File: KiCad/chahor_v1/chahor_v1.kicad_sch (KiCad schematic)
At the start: 12 parts, among them SW1 RotaryEncoder, SW2 lower_case, SW3 upper_case, SW4 space, SW5 bcksp, SW6 ctrl, SW7 switch, SW8 navi_up, SW9 navi_down, U1 Keyboard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

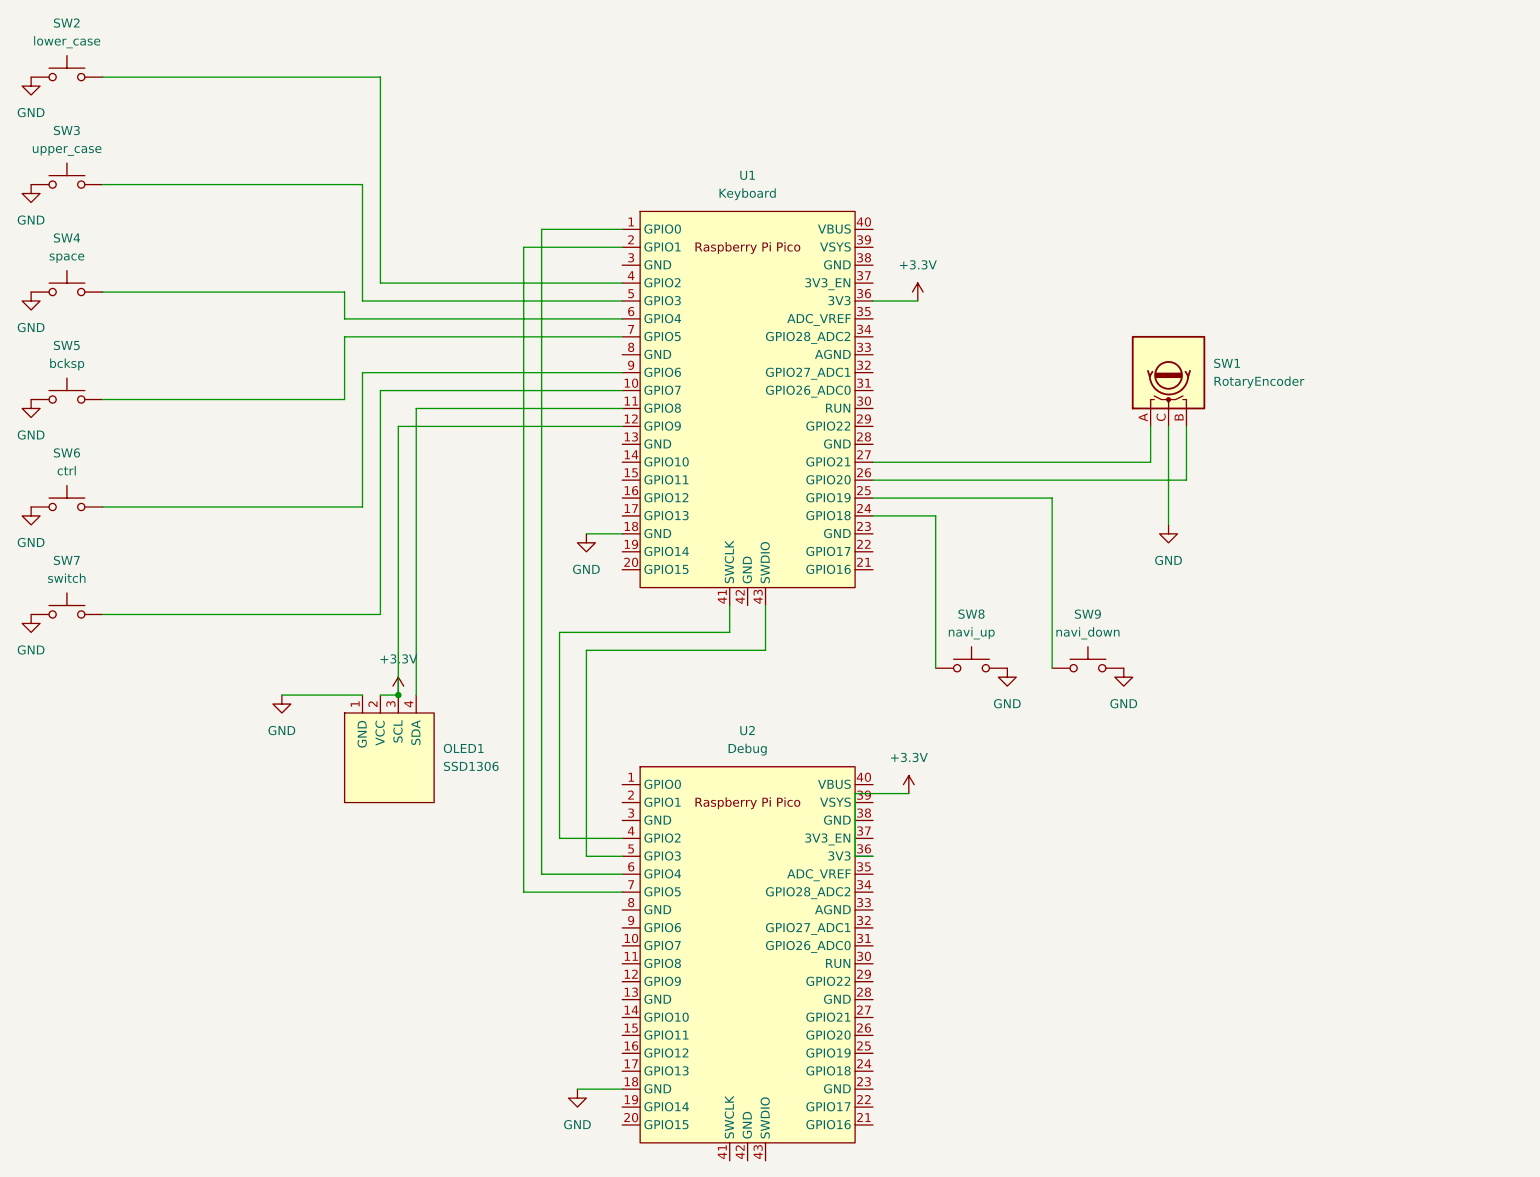
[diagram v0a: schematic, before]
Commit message: changed the production board to RP2040-Tiny
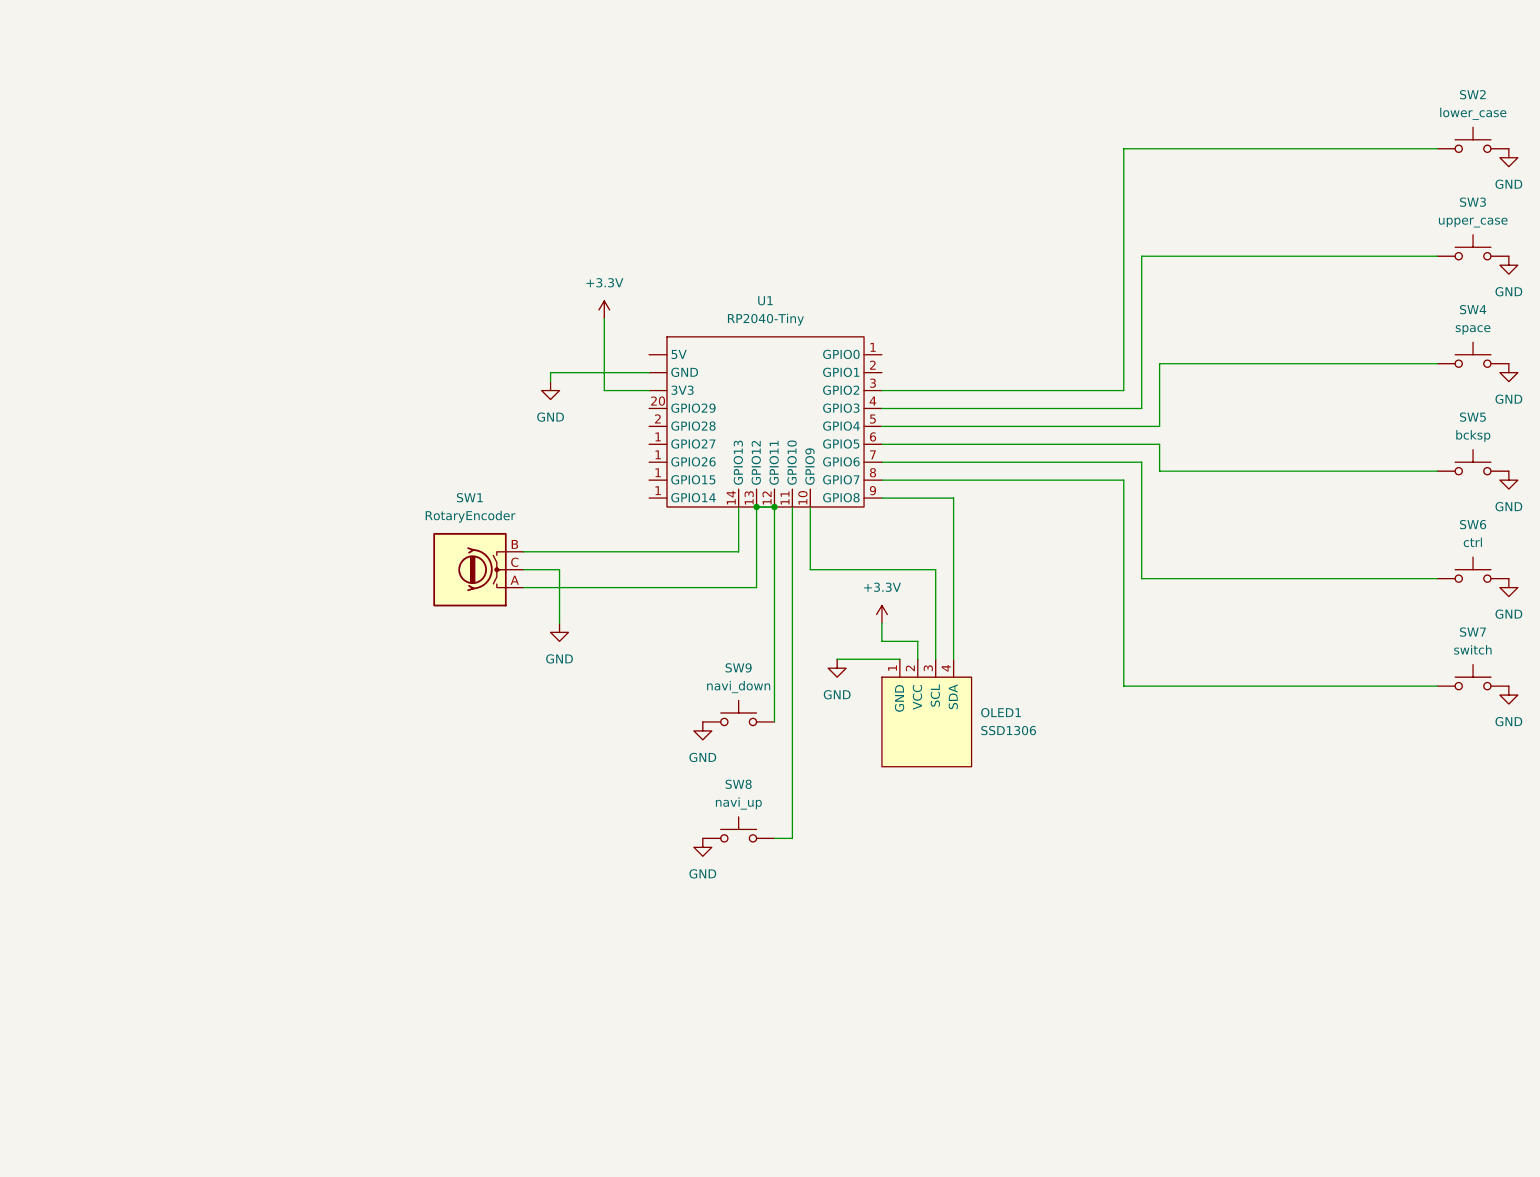
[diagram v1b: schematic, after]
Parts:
- removed U1: Keyboard, RPi_Pico:RPi_Pico_SMD_TH, symbol rp2040-pico:Pico
- removed U2: Debug, RPi_Pico:RPi_Pico_SMD_TH, symbol rp2040-pico:Pico
- added U1: RP2040-Tiny, symbol RP2040-Tiny:RP2040-Tiny
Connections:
- net +3.3V: now also U1. (3V3); no longer OLED1.3 (SCL)
- net GND: now also U1. (3V3)
- net at SW5.2: now also U1.6 (GPIO5)
- net at SW7.2: now also U1.8 (GPIO7)
- net at OLED1.4 (SDA): now also U1.9 (GPIO8)
- net at SW8.1: now also U1.11 (GPIO10)
- net at SW9.1: now also SW1.A, U1.12 (GPIO11), U1.13 (GPIO12)
- net at SW1.B: now also U1.14 (GPIO13)
- net at SW2.2: now also U1.3 (GPIO2)
- net at SW3.2: now also U1.4 (GPIO3)
- net at SW4.2: now also U1.5 (GPIO4)
- net at SW6.2: now also U1.7 (GPIO6)
- new net: OLED1.3 (SCL), U1.10 (GPIO9)
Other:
- moved on the sheet: OLED1, SW1, SW2, SW3, SW4, SW5, SW6, SW7, SW8, SW9
